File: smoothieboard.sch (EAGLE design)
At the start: 236 parts, among them IC1 LPC1769, IC10 LM1117-3.3V, IC2 A4982, IC3 A4982, IC4 MCP44X1, IC5 A4982, IC6 A4982, IC9 78L12Z, J10 POWER_JACKSMD, J5 POWER_JACKSMD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

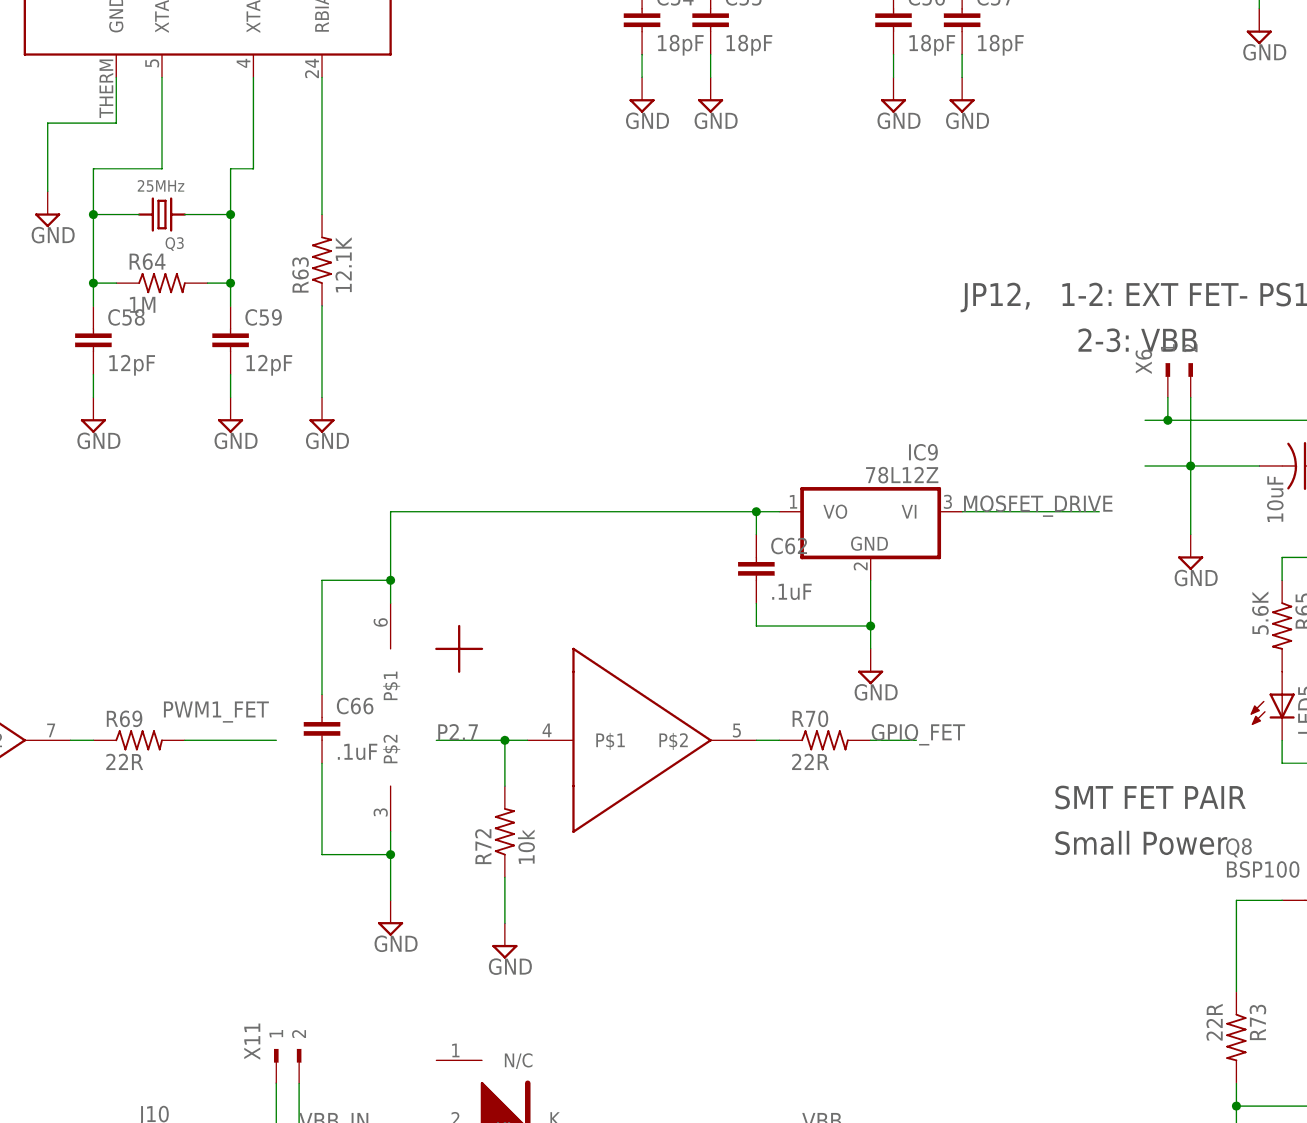
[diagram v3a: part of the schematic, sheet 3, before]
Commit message: switch 78L12Z for 78L12F surface mount package. also route remaining ratsnest wires- all were traces contacting pad, just not connected to center of pad
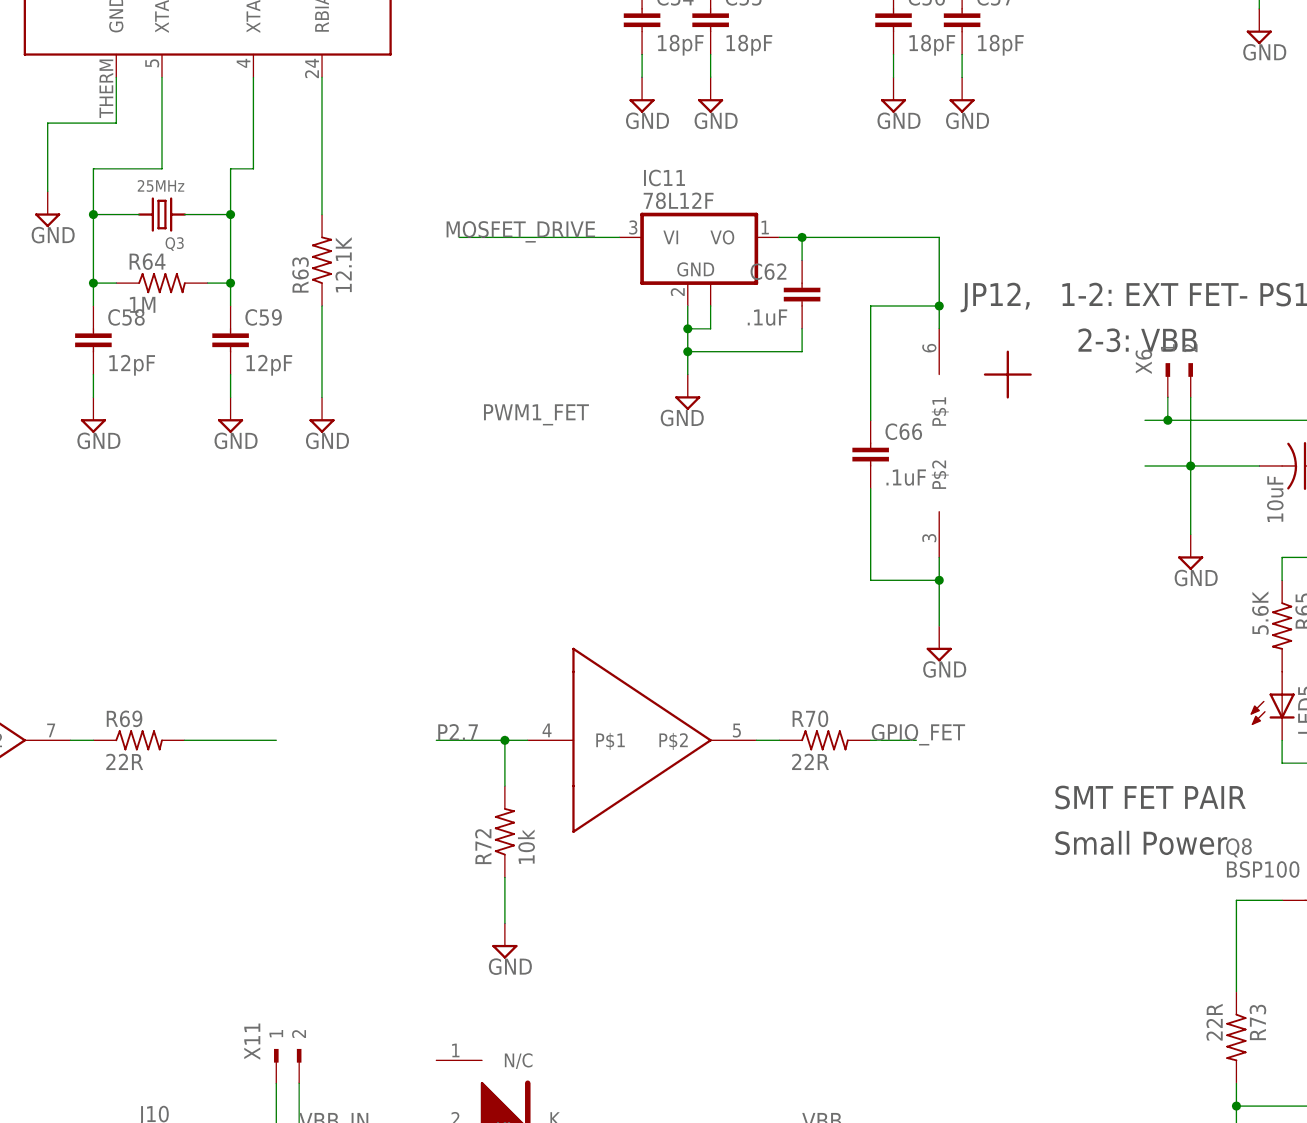
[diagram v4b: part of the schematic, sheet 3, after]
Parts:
- removed IC9: 78L12Z, linear:78L05Z
- added IC11: 78L12F, linear:78L12F
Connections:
- net 12VREG: now also IC11.VO; no longer IC9.VO
- net GND: now also IC11.GND, IC11.GND@1; no longer IC9.GND
- net MOSFET_DRIVE: now also IC11.VI; no longer IC9.VI
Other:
- moved on the sheet: C62, C66
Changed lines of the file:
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@@
 <part name="SUPPLY71" library="supply2" deviceset="GND" device=""/>
 <part name="SUPPLY72" library="supply2" deviceset="GND" device=""/>
-<part name="IC9" library="linear" deviceset="78*" device="Z" technology="L05" value="78L12Z"/>
 <part name="SUPPLY73" library="supply2" deviceset="GND" device=""/>
 <part name="C62" library="resistor" deviceset="C-EU" device="C0603" value=".1uF"/>
@@
 <part name="AGND3" library="supply1" deviceset="AGND" device=""/>
 <part name="C67" library="resistor" deviceset="C-EU" device="C0805" value="1uF"/>
+<part name="IC11" library="linear" deviceset="78L*" device="F" technology="12"/>
 </parts>
 <sheets>
@@
 </instance>
 <instance part="SUPPLY71" gate="GND" x="73.66" y="63.5"/>
-<instance part="SUPPLY72" gate="GND" x="137.16" y="66.04"/>
-<instance part="IC9" gate="A1" x="190.5" y="111.76" rot="MR0"/>
-<instance part="SUPPLY73" gate="GND" x="190.5" y="93.98"/>
-<instance part="C62" gate="G$1" x="177.8" y="106.68"/>
+<instance part="SUPPLY72" gate="GND" x="198.12" y="96.52"/>
+<instance part="SUPPLY73" gate="GND" x="170.18" y="124.46" rot="MR0"/>
+<instance part="C62" gate="G$1" x="182.88" y="137.16" rot="MR0"/>
 <instance part="SUPPLY78" gate="GND" x="149.86" y="63.5"/>
-<instance part="C66" gate="G$1" x="129.54" y="88.9"/>
-<instance part="U$2" gate="RAILS" x="137.16" y="88.9"/>
+<instance part="C66" gate="G$1" x="190.5" y="119.38"/>
+<instance part="U$2" gate="RAILS" x="198.12" y="119.38"/>
 <instance part="U$2" gate="A" x="86.36" y="86.36"/>
 <instance part="U$2" gate="B" x="162.56" y="86.36"/>
+<instance part="IC11" gate="G$1" x="170.18" y="142.24"/>
 </instances>
 <busses>
@@
 </segment>
 <segment>
-<pinref part="IC9" gate="A1" pin="GND"/>
 <pinref part="SUPPLY73" gate="GND" pin="GND"/>
-<wire x1="190.5" y1="96.52" x2="190.5" y2="99.06" width="0.1524" layer="91"/>
+<wire x1="170.18" y1="127" x2="170.18" y2="129.54" width="0.1524" layer="91"/>
 <pinref part="C62" gate="G$1" pin="2"/>
-<wire x1="190.5" y1="99.06" x2="190.5" y2="104.14" width="0.1524" layer="91"/>
-<wire x1="177.8" y1="101.6" x2="177.8" y2="99.06" width="0.1524" layer="91"/>
-<wire x1="177.8" y1="99.06" x2="190.5" y2="99.06" width="0.1524" layer="91"/>
-<junction x="190.5" y="99.06"/>
+<wire x1="170.18" y1="129.54" x2="170.18" y2="132.08" width="0.1524" layer="91"/>
+<wire x1="170.18" y1="132.08" x2="170.18" y2="134.62" width="0.1524" layer="91"/>
+<wire x1="182.88" y1="132.08" x2="182.88" y2="129.54" width="0.1524" layer="91"/>
+<wire x1="182.88" y1="129.54" x2="170.18" y2="129.54" width="0.1524" layer="91"/>
+<junction x="170.18" y="129.54"/>
+<pinref part="IC11" gate="G$1" pin="GND"/>
+<pinref part="IC11" gate="G$1" pin="GND@1"/>
+<wire x1="170.18" y1="132.08" x2="172.72" y2="132.08" width="0.1524" layer="91"/>
+<wire x1="172.72" y1="132.08" x2="172.72" y2="134.62" width="0.1524" layer="91"/>
+<junction x="170.18" y="132.08"/>
 </segment>
 <segment>
 <pinref part="SUPPLY72" gate="GND" pin="GND"/>
 <pinref part="C66" gate="G$1" pin="2"/>
-<wire x1="129.54" y1="83.82" x2="129.54" y2="73.66" width="0.1524" layer="91"/>
-<wire x1="129.54" y1="73.66" x2="137.16" y2="73.66" width="0.1524" layer="91"/>
-<wire x1="137.16" y1="73.66" x2="137.16" y2="68.58" width="0.1524" layer="91"/>
+<wire x1="190.5" y1="114.3" x2="190.5" y2="104.14" width="0.1524" layer="91"/>
+<wire x1="190.5" y1="104.14" x2="198.12" y2="104.14" width="0.1524" layer="91"/>
+<wire x1="198.12" y1="104.14" x2="198.12" y2="99.06" width="0.1524" layer="91"/>
 <pinref part="U$2" gate="RAILS" pin="P$2"/>
-<wire x1="137.16" y1="73.66" x2="137.16" y2="76.2" width="0.1524" layer="91"/>
-<junction x="137.16" y="73.66"/>
+<wire x1="198.12" y1="104.14" x2="198.12" y2="106.68" width="0.1524" layer="91"/>
+<junction x="198.12" y="104.14"/>
 </segment>
 <segment>
@@
 </segment>
 <segment>
-<pinref part="IC9" gate="A1" pin="VI"/>
-<label x="200.66" y="111.76" size="1.778" layer="95"/>
-<wire x1="200.66" y1="111.76" x2="215.9" y2="111.76" width="0.1524" layer="91"/>
+<label x="160.02" y="142.24" size="1.778" layer="95" rot="MR0"/>
+<wire x1="162.56" y1="142.24" x2="144.78" y2="142.24" width="0.1524" layer="91"/>
+<pinref part="IC11" gate="G$1" pin="VI"/>
 </segment>
 </net>
@@
 <net name="12VREG" class="0">
 <segment>
-<pinref part="IC9" gate="A1" pin="VO"/>
-<wire x1="180.34" y1="111.76" x2="177.8" y2="111.76" width="0.1524" layer="91"/>
+<wire x1="180.34" y1="142.24" x2="182.88" y2="142.24" width="0.1524" layer="91"/>
 <pinref part="C62" gate="G$1" pin="1"/>
-<wire x1="177.8" y1="109.22" x2="177.8" y2="111.76" width="0.1524" layer="91"/>
-<wire x1="137.16" y1="101.6" x2="137.16" y2="104.14" width="0.1524" layer="91"/>
-<wire x1="137.16" y1="104.14" x2="137.16" y2="111.76" width="0.1524" layer="91"/>
-<wire x1="137.16" y1="111.76" x2="177.8" y2="111.76" width="0.1524" layer="91"/>
-<junction x="177.8" y="111.76"/>
+<wire x1="182.88" y1="139.7" x2="182.88" y2="142.24" width="0.1524" layer="91"/>
+<wire x1="198.12" y1="132.08" x2="198.12" y2="134.62" width="0.1524" layer="91"/>
+<wire x1="198.12" y1="134.62" x2="198.12" y2="142.24" width="0.1524" layer="91"/>
+<wire x1="198.12" y1="142.24" x2="182.88" y2="142.24" width="0.1524" layer="91"/>
+<junction x="182.88" y="142.24"/>
 <pinref part="C66" gate="G$1" pin="1"/>
-<wire x1="129.54" y1="91.44" x2="129.54" y2="104.14" width="0.1524" layer="91"/>
-<wire x1="129.54" y1="104.14" x2="137.16" y2="104.14" width="0.1524" layer="91"/>
-<junction x="137.16" y="104.14"/>
+<wire x1="190.5" y1="121.92" x2="190.5" y2="134.62" width="0.1524" layer="91"/>
+<wire x1="190.5" y1="134.62" x2="198.12" y2="134.62" width="0.1524" layer="91"/>
+<junction x="198.12" y="134.62"/>
 <pinref part="U$2" gate="RAILS" pin="P$1"/>
+<pinref part="IC11" gate="G$1" pin="VO"/>
 </segment>
 </net>
@@
 <pinref part="R69" gate="G$1" pin="2"/>
 <wire x1="114.3" y1="86.36" x2="124.46" y2="86.36" width="0.1524" layer="91"/>
-<label x="111.76" y="88.9" size="1.778" layer="95"/>
+<label x="147.32" y="121.92" size="1.778" layer="95"/>
 </segment>
 <segment>

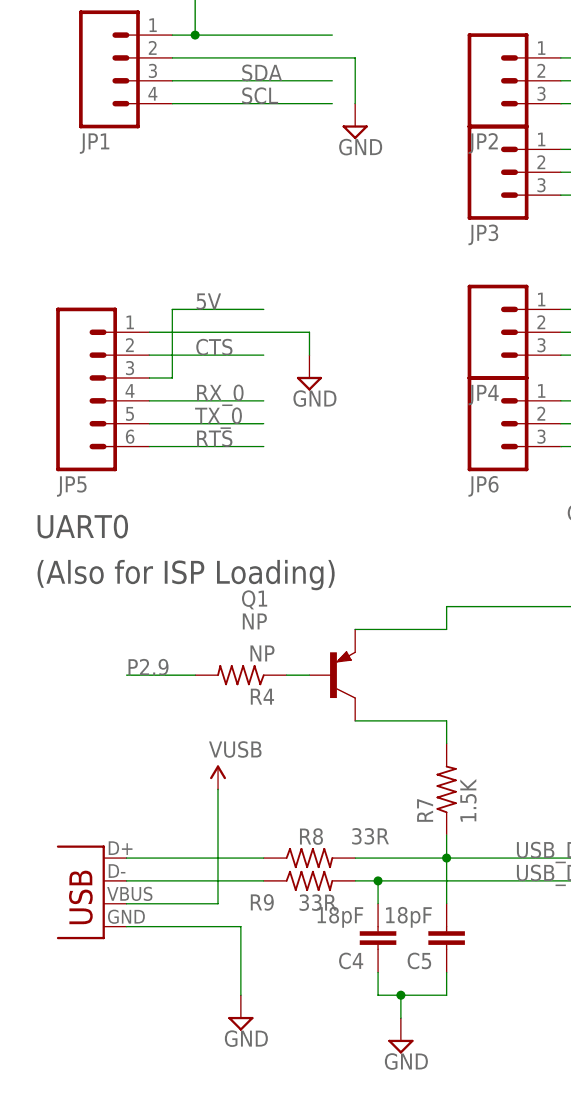
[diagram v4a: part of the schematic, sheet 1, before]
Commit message: USB-B connector, solder jumper for 5v/3v3 UART power (NOT signals, they're always 3v3)
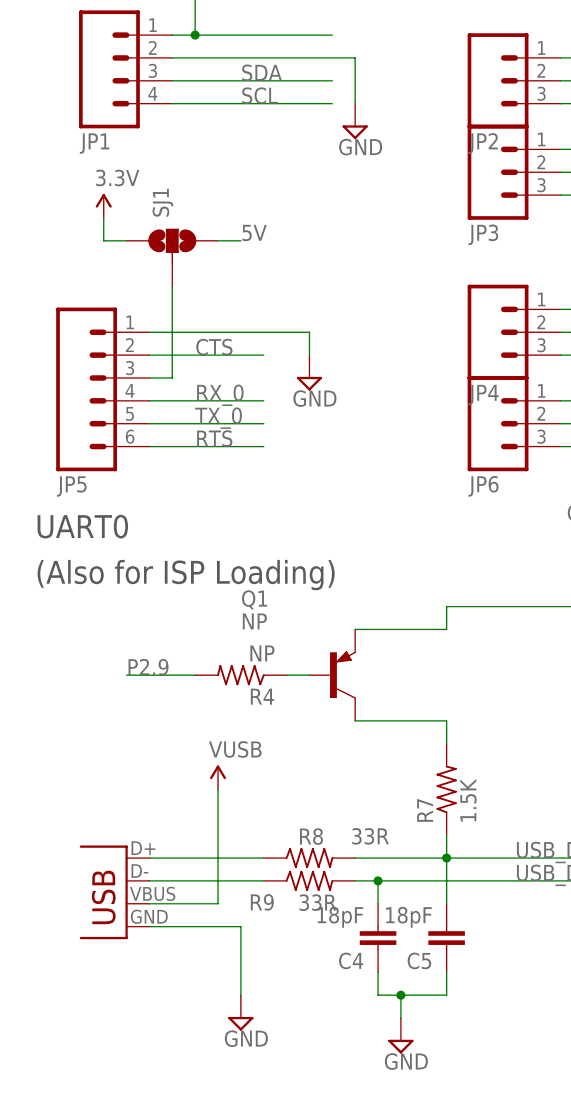
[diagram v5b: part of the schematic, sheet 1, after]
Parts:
- removed X13: USBPTH, SparkFun:USBPTH
- added SJ1: (no value), SparkFun:SOLDERJUMPER_2WAYS
- added X14: USBPTH, SparkFun:USBPTH
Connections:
- new net N$23: JP5.3, SJ1.2
- net 3.3V: now also SJ1.1
- net 5V: now also SJ1.3; no longer JP5.3
- net GND: now also X14.GND; no longer X13.GND
- net N$61: now also X14.D+; no longer X13.D+
- net N$62: now also X14.D-; no longer X13.D-
- net VUSB: now also X14.VBUS; no longer X13.VBUS
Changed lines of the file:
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@@
 <part name="JP31" library="SparkFun" deviceset="JUMPER-2" device="SMD-NC"/>
 <part name="U$2" library="custom_esorensen" deviceset="TC4427" device=""/>
-<part name="X13" library="SparkFun" deviceset="USB" device="PTH"/>
 <part name="AGND1" library="supply1" deviceset="AGND" device=""/>
 <part name="AGND2" library="supply1" deviceset="AGND" device=""/>
@@
 <part name="C67" library="resistor" deviceset="C-EU" device="C0805" value="1uF"/>
 <part name="IC11" library="linear" deviceset="78L*" device="F" technology="12"/>
+<part name="X14" library="SparkFun" deviceset="USB" device="PTH"/>
+<part name="SJ1" library="SparkFun" deviceset="SOLDERJUMPER_2WAY" device="S"/>
+<part name="P+23" library="SparkFun" deviceset="3.3V" device=""/>
 </parts>
 <sheets>
@@
 <instance part="JP15" gate="G$1" x="294.64" y="124.46" rot="R180"/>
 <instance part="JP29" gate="G$1" x="73.66" y="104.14" rot="R180"/>
-<instance part="X13" gate="G$1" x="20.32" y="144.78" rot="MR0"/>
 <instance part="AGND1" gate="VR1" x="226.06" y="106.68"/>
 <instance part="AGND2" gate="VR1" x="241.3" y="78.74"/>
 <instance part="C67" gate="G$1" x="340.36" y="226.06" rot="R180"/>
+<instance part="X14" gate="G$1" x="22.86" y="144.78" rot="MR0"/>
+<instance part="SJ1" gate="G$1" x="27.94" y="220.98" rot="R90"/>
+<instance part="P+23" gate="G$1" x="20.32" y="223.52"/>
 </instances>
 <busses>
@@
 <wire x1="35.56" y1="144.78" x2="35.56" y2="137.16" width="0.1524" layer="91"/>
 <pinref part="SUPPLY28" gate="GND" pin="GND"/>
-<pinref part="X13" gate="G$1" pin="GND"/>
-<wire x1="35.56" y1="144.78" x2="22.86" y2="144.78" width="0.1524" layer="91"/>
+<wire x1="35.56" y1="144.78" x2="25.4" y2="144.78" width="0.1524" layer="91"/>
+<pinref part="X14" gate="G$1" pin="GND"/>
 </segment>
 <segment>
@@
 <wire x1="81.28" y1="213.36" x2="81.28" y2="220.98" width="0.1524" layer="91"/>
 </segment>
+<segment>
+<pinref part="SJ1" gate="G$1" pin="1"/>
+<pinref part="P+23" gate="G$1" pin="3.3V"/>
+<wire x1="22.86" y1="220.98" x2="20.32" y2="220.98" width="0.1524" layer="91"/>
+<wire x1="20.32" y1="220.98" x2="20.32" y2="223.52" width="0.1524" layer="91"/>
+</segment>
 </net>
 <net name="AVCC" class="0">
@@
 <segment>
 <pinref part="R8" gate="G$1" pin="1"/>
-<pinref part="X13" gate="G$1" pin="D+"/>
-<wire x1="22.86" y1="152.4" x2="38.1" y2="152.4" width="0.1524" layer="91"/>
+<wire x1="25.4" y1="152.4" x2="38.1" y2="152.4" width="0.1524" layer="91"/>
+<pinref part="X14" gate="G$1" pin="D+"/>
 </segment>
 </net>
@@
 <segment>
 <pinref part="R9" gate="G$1" pin="1"/>
-<pinref part="X13" gate="G$1" pin="D-"/>
-<wire x1="22.86" y1="149.86" x2="38.1" y2="149.86" width="0.1524" layer="91"/>
+<wire x1="25.4" y1="149.86" x2="38.1" y2="149.86" width="0.1524" layer="91"/>
+<pinref part="X14" gate="G$1" pin="D-"/>
 </segment>
 </net>
@@
 <pinref part="VUSB" gate="G$1" pin="5V"/>
 <wire x1="33.02" y1="160.02" x2="33.02" y2="147.32" width="0.1524" layer="91"/>
-<pinref part="X13" gate="G$1" pin="VBUS"/>
-<wire x1="33.02" y1="147.32" x2="22.86" y2="147.32" width="0.1524" layer="91"/>
+<wire x1="33.02" y1="147.32" x2="25.4" y2="147.32" width="0.1524" layer="91"/>
+<pinref part="X14" gate="G$1" pin="VBUS"/>
 </segment>
 </net>
@@
 <net name="5V" class="0">
 <segment>
-<pinref part="JP5" gate="G$1" pin="3"/>
-<wire x1="25.4" y1="205.74" x2="27.94" y2="205.74" width="0.1524" layer="91"/>
-<wire x1="27.94" y1="205.74" x2="27.94" y2="213.36" width="0.1524" layer="91"/>
-<wire x1="27.94" y1="213.36" x2="38.1" y2="213.36" width="0.1524" layer="91"/>
-<label x="30.48" y="213.36" size="1.778" layer="95"/>
+<wire x1="33.02" y1="220.98" x2="35.56" y2="220.98" width="0.1524" layer="91"/>
+<label x="35.56" y="220.98" size="1.778" layer="95"/>
+<pinref part="SJ1" gate="G$1" pin="3"/>
 </segment>
 </net>
@@
 </segment>
 </net>
+<net name="N$23" class="0">
+<segment>
+<pinref part="JP5" gate="G$1" pin="3"/>
+<pinref part="SJ1" gate="G$1" pin="2"/>
+<wire x1="25.4" y1="205.74" x2="27.94" y2="205.74" width="0.1524" layer="91"/>
+<wire x1="27.94" y1="205.74" x2="27.94" y2="215.9" width="0.1524" layer="91"/>
+</segment>
+</net>
